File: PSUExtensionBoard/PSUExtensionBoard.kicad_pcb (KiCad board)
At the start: 2 copper layers, 149.9 x 50.8 mm, 14 parts

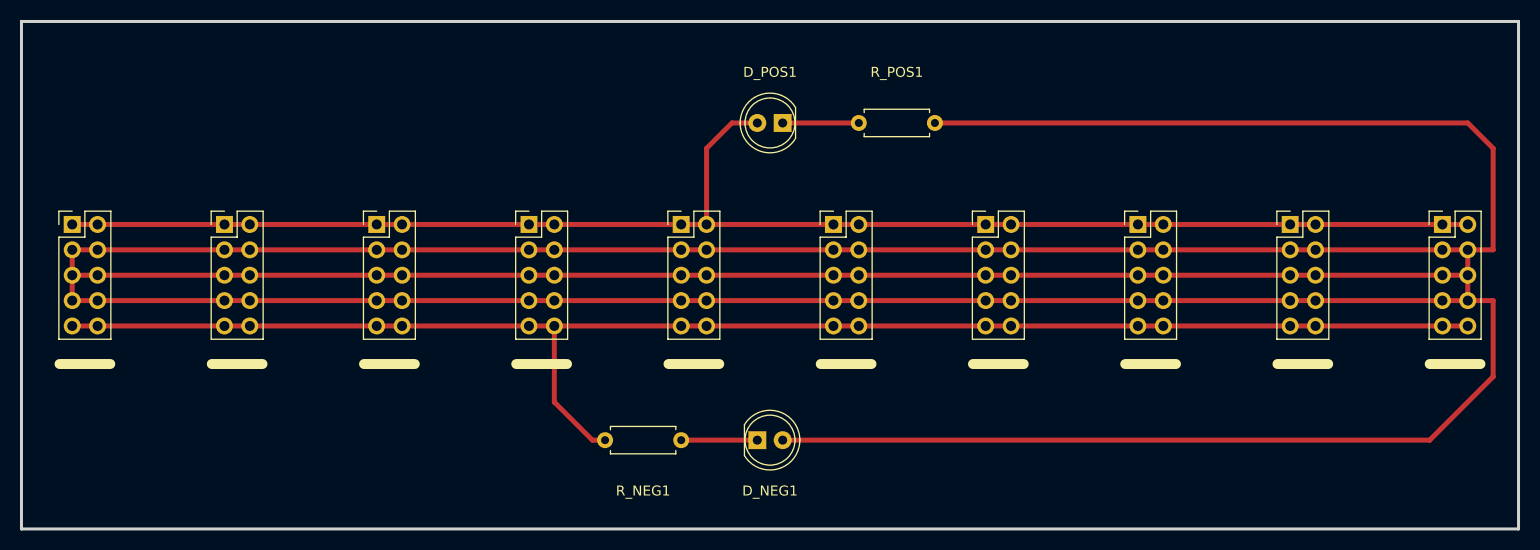
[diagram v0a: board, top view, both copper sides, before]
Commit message: Changed Ext Board to add 5V, CV, Gate
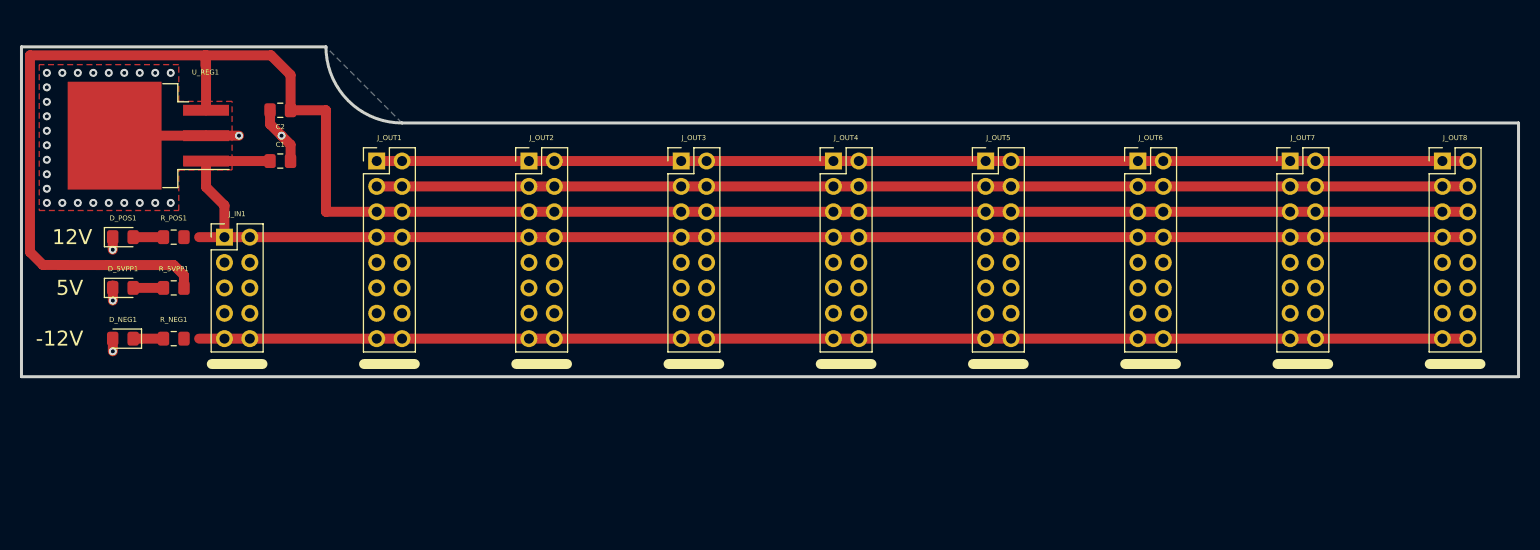
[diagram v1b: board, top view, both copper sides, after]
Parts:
- removed J_OUT10, J_OUT9: Conn_02x05_Odd_Even, Connector_PinHeader_2.54mm:PinHeader_2x05_P2.54mm_Vertical
- added C1: 220nF, Capacitor_SMD:C_0805_2012Metric_Pad1.15x1.40mm_HandSolder, F.Cu at (74.2, 92.7)
- added C2: 100nF, Capacitor_SMD:C_0805_2012Metric_Pad1.15x1.40mm_HandSolder, F.Cu at (74.2, 87.6)
- added D_5VPP1: LED, LED_SMD:LED_0805_2012Metric_Pad1.15x1.40mm_HandSolder, F.Cu at (58.4, 105.4)
- added J_IN1: Conn_02x05_Odd_Even, Connector_PinHeader_2.54mm:PinHeader_2x05_P2.54mm_Vertical, F.Cu at (68.6, 100.3)
- added R_5VPP1: 2K7, Resistor_SMD:R_0805_2012Metric_Pad1.15x1.40mm_HandSolder, F.Cu at (63.5, 105.4)
- added U_REG1: L7805, Package_TO_SOT_SMD:TO-263-3_TabPin2, F.Cu at (61.0, 90.2)
- D_NEG1, D_POS1: footprint LED_THT:LED_D5.0mm -> LED_SMD:LED_0805_2012Metric_Pad1.15x1.40mm_HandSolder
- J_OUT1, J_OUT2, J_OUT3, J_OUT4, J_OUT5, J_OUT6, J_OUT7, J_OUT8: value Conn_02x05_Odd_Even -> Conn_02x08_Odd_Even; footprint Connector_PinHeader_2.54mm:PinHeader_2x05_P2.54mm_Vertical -> Connector_PinHeader_2.54mm:PinHeader_2x08_P2.54mm_Vertical
- R_NEG1, R_POS1: value 1K -> 2K7; footprint Resistor_THT:R_Axial_DIN0207_L6.3mm_D2.5mm_P7.62mm_Horizontal -> Resistor_SMD:R_0805_2012Metric_Pad1.15x1.40mm_HandSolder
- moved R_POS1 69.5 mm to (63.5, 100.3), turned to 180 degrees
- moved D_POS1 67.0 mm to (58.4, 100.3), turned to 0 degrees
- moved D_NEG1 64.3 mm to (58.4, 110.5), turned to 180 degrees
- moved R_NEG1 51.8 mm to (63.5, 110.5), turned to 0 degrees
- moved J_OUT6 31.1 mm to (160.0, 92.7)
- moved J_OUT2 31.1 mm to (99.1, 92.7)
- moved J_OUT3 31.1 mm to (114.3, 92.7)
- moved J_OUT5 31.1 mm to (144.8, 92.7)
- moved J_OUT1 31.1 mm to (83.8, 92.7)
- moved J_OUT4 31.1 mm to (129.5, 92.7)
- moved J_OUT7 31.1 mm to (175.3, 92.7)
- moved J_OUT8 31.1 mm to (190.5, 92.7)
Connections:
- D_POS1 pad 1: Net-(D_POS1-Pad1) -> GND
- J_OUT1 pad 1: Net-(D_POS1-Pad2) -> /GATE
- J_OUT1 pad 10: Net-(J_OUT1-Pad10) -> GND
- J_OUT1 pad 2: Net-(D_POS1-Pad2) -> /GATE
- J_OUT1 pad 3: GND -> /CV
- J_OUT1 pad 4: GND -> /CV
- J_OUT1 pad 5: GND -> /5V
- J_OUT1 pad 6: GND -> /5V
- J_OUT1 pad 7: GND -> /12V
- J_OUT1 pad 8: GND -> /12V
- J_OUT1 pad 9: Net-(J_OUT1-Pad10) -> GND
- J_OUT2 pad 1: Net-(D_POS1-Pad2) -> /GATE
- J_OUT2 pad 10: Net-(J_OUT1-Pad10) -> GND
- J_OUT2 pad 2: Net-(D_POS1-Pad2) -> /GATE
- J_OUT2 pad 3: GND -> /CV
- J_OUT2 pad 4: GND -> /CV
- J_OUT2 pad 5: GND -> /5V
- J_OUT2 pad 6: GND -> /5V
- J_OUT2 pad 7: GND -> /12V
- J_OUT2 pad 8: GND -> /12V
- J_OUT2 pad 9: Net-(J_OUT1-Pad10) -> GND
- J_OUT3 pad 1: Net-(D_POS1-Pad2) -> /GATE
- J_OUT3 pad 10: Net-(J_OUT1-Pad10) -> GND
- J_OUT3 pad 2: Net-(D_POS1-Pad2) -> /GATE
- J_OUT3 pad 3: GND -> /CV
- J_OUT3 pad 4: GND -> /CV
- J_OUT3 pad 5: GND -> /5V
- J_OUT3 pad 6: GND -> /5V
- J_OUT3 pad 7: GND -> /12V
- J_OUT3 pad 8: GND -> /12V
- J_OUT3 pad 9: Net-(J_OUT1-Pad10) -> GND
- J_OUT4 pad 1: Net-(D_POS1-Pad2) -> /GATE
- J_OUT4 pad 10: Net-(J_OUT1-Pad10) -> GND
- J_OUT4 pad 2: Net-(D_POS1-Pad2) -> /GATE
- J_OUT4 pad 3: GND -> /CV
- J_OUT4 pad 4: GND -> /CV
- J_OUT4 pad 5: GND -> /5V
- J_OUT4 pad 6: GND -> /5V
- J_OUT4 pad 7: GND -> /12V
- J_OUT4 pad 8: GND -> /12V
- J_OUT4 pad 9: Net-(J_OUT1-Pad10) -> GND
- J_OUT5 pad 1: Net-(D_POS1-Pad2) -> /GATE
- J_OUT5 pad 10: Net-(J_OUT1-Pad10) -> GND
- J_OUT5 pad 2: Net-(D_POS1-Pad2) -> /GATE
- J_OUT5 pad 3: GND -> /CV
- J_OUT5 pad 4: GND -> /CV
- J_OUT5 pad 5: GND -> /5V
- J_OUT5 pad 6: GND -> /5V
- J_OUT5 pad 7: GND -> /12V
- J_OUT5 pad 8: GND -> /12V
- J_OUT5 pad 9: Net-(J_OUT1-Pad10) -> GND
- J_OUT6 pad 1: Net-(D_POS1-Pad2) -> /GATE
- J_OUT6 pad 10: Net-(J_OUT1-Pad10) -> GND
- J_OUT6 pad 2: Net-(D_POS1-Pad2) -> /GATE
- J_OUT6 pad 3: GND -> /CV
- J_OUT6 pad 4: GND -> /CV
- J_OUT6 pad 5: GND -> /5V
- J_OUT6 pad 6: GND -> /5V
- J_OUT6 pad 7: GND -> /12V
- J_OUT6 pad 8: GND -> /12V
- J_OUT6 pad 9: Net-(J_OUT1-Pad10) -> GND
- J_OUT7 pad 1: Net-(D_POS1-Pad2) -> /GATE
- J_OUT7 pad 10: Net-(J_OUT1-Pad10) -> GND
- J_OUT7 pad 2: Net-(D_POS1-Pad2) -> /GATE
- J_OUT7 pad 3: GND -> /CV
- J_OUT7 pad 4: GND -> /CV
- J_OUT7 pad 5: GND -> /5V
- J_OUT7 pad 6: GND -> /5V
- J_OUT7 pad 7: GND -> /12V
- J_OUT7 pad 8: GND -> /12V
- J_OUT7 pad 9: Net-(J_OUT1-Pad10) -> GND
- J_OUT8 pad 1: Net-(D_POS1-Pad2) -> /GATE
- J_OUT8 pad 10: Net-(J_OUT1-Pad10) -> GND
- J_OUT8 pad 2: Net-(D_POS1-Pad2) -> /GATE
- J_OUT8 pad 3: GND -> /CV
- J_OUT8 pad 4: GND -> /CV
- J_OUT8 pad 5: GND -> /5V
- J_OUT8 pad 6: GND -> /5V
- J_OUT8 pad 7: GND -> /12V
- J_OUT8 pad 8: GND -> /12V
- J_OUT8 pad 9: Net-(J_OUT1-Pad10) -> GND
- R_NEG1 pad 2: Net-(J_OUT1-Pad10) -> /-12V
- R_POS1 pad 1: Net-(D_POS1-Pad1) -> /12V
- R_POS1 pad 2: GND -> Net-(D_POS1-Pad2)
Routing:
- net GND: track 582.8 -> 22.4 mm, vias 0 -> 31
- net /5V: track 0.00 -> 202.4 mm
- net Net-(J_OUT1-Pad10): track 154.0 -> 0.00 mm
- net Net-(D_POS1-Pad2): track 153.5 -> 2.54 mm
- net /12V: track 0.00 -> 141.8 mm
- net /-12V: track 0.00 -> 127.0 mm
- net /GATE: track 0.00 -> 109.2 mm
- net /CV: track 0.00 -> 109.2 mm
- net Net-(D_POS1-Pad1): track 7.62 -> 0.00 mm
- net Net-(D_NEG1-Pad1): track 7.62 -> 2.78 mm
- net Net-(D_5VPP1-Pad2): track 0.00 -> 3.03 mm
- added copper zone on B.Cu, net GND
- added copper zone on F.Cu, net GND
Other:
- board size 149.9 x 50.8 mm -> 149.9 x 33 mm
- board text added: "-12V"
- board text added: "12V"
- board text added: "5V"

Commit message: Created SMT version of AdjustablePSU, RevB
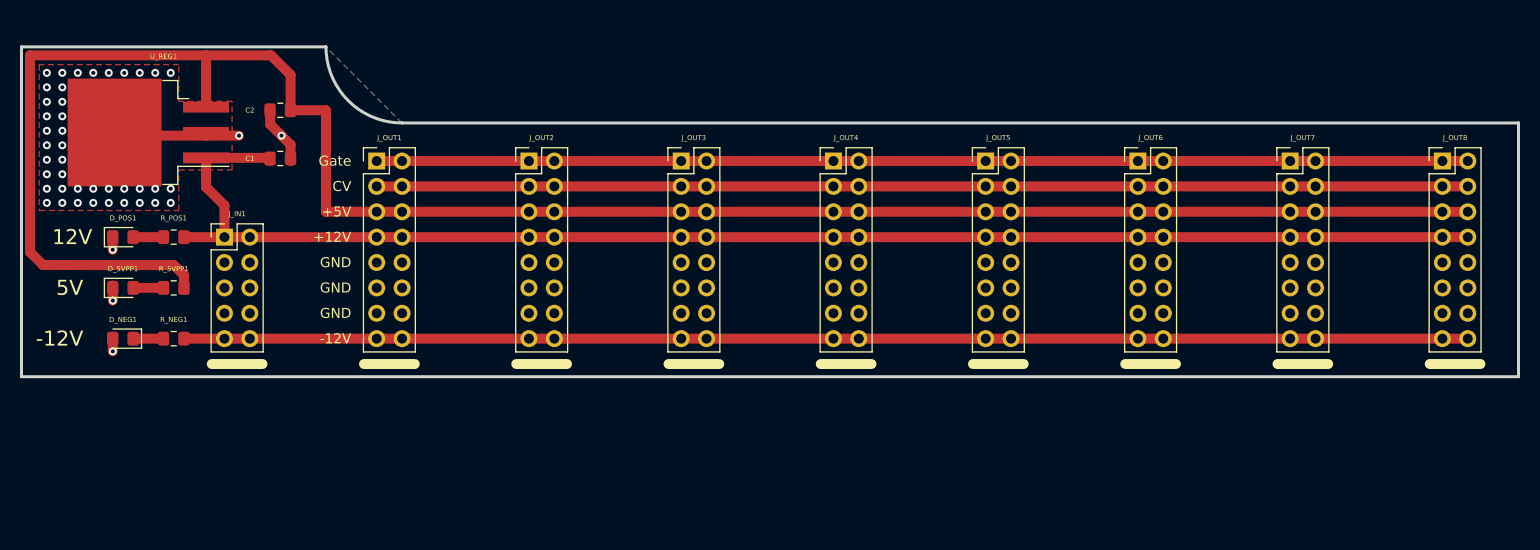
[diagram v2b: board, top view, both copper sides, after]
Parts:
- moved U_REG1 0.32 mm to (61.0, 89.9)
- moved C1 0.25 mm to (74.2, 92.5)
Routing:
- net /12V: track 141.8 -> 143.6 mm
- net /-12V: track 127.0 -> 128.5 mm
- net /5V: track 202.4 -> 201.0 mm
- net GND: vias 31 -> 46
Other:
- board text added: "+/-12V, +5V, CV and Gate"
- board text added: "+12V"
- board text added: "+5V"
- board text added: "CV"
- board text added: "Eurorack PSU Ext. board"
- board text added: "GND"
- board text added: "Gate"
- board text added: "RevA Chris Sutton 2018"
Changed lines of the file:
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@@
   (general
     (thickness 1.6)
-    (drawings 18)
-    (tracks 67)
+    (drawings 29)
+    (tracks 82)
     (zones 0)
     (modules 18)
@@
   )
   (setup
-    (last_trace_width 1)
+    (last_trace_width 0.25)
     (user_trace_width 0.5)
     (user_trace_width 1)
@@
       (outputformat 1)
       (mirror false)
-      (drillshape 1)
+      (drillshape 0)
       (scaleselection 1)
-      (outputdirectory ""))
+      (outputdirectory "PSUEXT_GERBER/"))
   )
   (net 0 "")
@@
   )
   (module Package_TO_SOT_SMD:TO-263-3_TabPin2 (layer F.Cu)
-    (at 60.96 90.17 180)
+    (at 60.96 89.8525 180)
     (descr "TO-263 / D2PAK / DDPAK SMD package, http://www.infineon.com/cms/en/product/packages/PG-TO263/PG-TO263-3-1/")
     (tags "D2PAK DDPAK TO-263 D2PAK-3 TO-263-3 SOT-404")
     (attr smd)
-    (fp_text reference U_REG1 (at -5.715 6.35 180) (layer F.SilkS)
+    (fp_text reference U_REG1 (at -1.524 7.62 180) (layer F.SilkS)
       (effects (font (size 0.5 0.5) (thickness 0.1)))
     )
@@
   )
   (module Capacitor_SMD:C_0805_2012Metric_Pad1.15x1.40mm_HandSolder (layer F.Cu)
-    (at 74.168 92.71)
+    (at 74.168 92.456)
     (descr "Capacitor SMD 0805 (2012 Metric), square (rectangular) end terminal, IPC_7351 nominal with elongated pad for handsoldering. (Body size source: https://docs.google.com/spreadsheets/d/1BsfQQcO9C6DZCsRaXUlFlo91Tg2WpOkGARC1WS5S8t0/edit?usp=sharing), generated with kicad-footprint-generator")
     (tags "capacitor handsolder")
     (attr smd)
-    (fp_text reference C1 (at 0 -1.65) (layer F.SilkS)
+    (fp_text reference C1 (at -3.048 0) (layer F.SilkS)
       (effects (font (size 0.5 0.5) (thickness 0.1)))
     )
@@
     (tags "capacitor handsolder")
     (attr smd)
-    (fp_text reference C2 (at 0 -1.65 180) (layer F.SilkS)
+    (fp_text reference C2 (at 3.048 0 180) (layer F.SilkS)
       (effects (font (size 0.5 0.5) (thickness 0.1)))
     )
@@
     )
   )
+  (gr_text -12V (at 81.28 110.49) (layer F.SilkS)
+    (effects (font (size 1 1) (thickness 0.2)) (justify right))
+  )
+  (gr_text GND (at 81.28 107.95) (layer F.SilkS)
+    (effects (font (size 1 1) (thickness 0.2)) (justify right))
+  )
+  (gr_text GND (at 81.28 105.41) (layer F.SilkS)
+    (effects (font (size 1 1) (thickness 0.2)) (justify right))
+  )
+  (gr_text GND (at 81.28 102.87) (layer F.SilkS)
+    (effects (font (size 1 1) (thickness 0.2)) (justify right))
+  )
+  (gr_text +12V (at 81.28 100.33) (layer F.SilkS)
+    (effects (font (size 1 1) (thickness 0.2)) (justify right))
+  )
+  (gr_text +5V (at 81.28 97.79) (layer F.SilkS)
+    (effects (font (size 1 1) (thickness 0.2)) (justify right))
+  )
+  (gr_text CV (at 81.28 95.25) (layer F.SilkS)
+    (effects (font (size 1 1) (thickness 0.2)) (justify right))
+  )
+  (gr_text Gate (at 81.28 92.71) (layer F.SilkS)
+    (effects (font (size 1 1) (thickness 0.2)) (justify right))
+  )
+  (gr_text "RevA Chris Sutton 2018" (at 80.2005 101.6 90) (layer B.SilkS)
+    (effects (font (size 1 1) (thickness 0.2)) (justify mirror))
+  )
+  (gr_text "+/-12V, +5V, CV and Gate" (at 77.47 101.6 90) (layer B.SilkS)
+    (effects (font (size 1 1) (thickness 0.2)) (justify mirror))
+  )
+  (gr_text "Eurorack PSU Ext. board" (at 74.93 101.6 90) (layer B.SilkS)
+    (effects (font (size 1 1) (thickness 0.2)) (justify mirror))
+  )
   (gr_line (start 48.26 81.28) (end 78.74 81.28) (layer Edge.Cuts) (width 0.3))
   (gr_line (start 86.36 88.9) (end 198.12 88.9) (layer Edge.Cuts) (width 0.3))
   (gr_arc (start 86.36 81.28) (end 78.74 81.28) (angle -90) (layer Edge.Cuts) (width 0.3))
   (gr_text -12V (at 52.07 110.49) (layer F.SilkS)
-    (effects (font (size 1.5 1.5) (thickness 0.3)))
+    (effects (font (size 1.5 1.5) (thickness 0.2)))
   )
   (gr_text 5V (at 53.086 105.41) (layer F.SilkS)
-    (effects (font (size 1.5 1.5) (thickness 0.3)))
+    (effects (font (size 1.5 1.5) (thickness 0.2)))
   )
   (gr_text 12V (at 53.34 100.33) (layer F.SilkS)
-    (effects (font (size 1.5 1.5) (thickness 0.3)))
+    (effects (font (size 1.5 1.5) (thickness 0.2)))
   )
   (gr_line (start 189.23 113.03) (end 194.31 113.03) (layer F.SilkS) (width 1))
@@
   (segment (start 57.404 105.165) (end 57.404 106.68) (width 1) (layer F.Cu) (net 1))
   (via (at 57.404 106.68) (size 0.8) (drill 0.4) (layers F.Cu B.Cu) (net 1))
+  (via (at 52.35 85.3335) (size 0.8) (drill 0.4) (layers F.Cu B.Cu) (net 1))
+  (via (at 52.35 86.7835) (size 0.8) (drill 0.4) (layers F.Cu B.Cu) (net 1))
+  (via (at 52.35 88.2335) (size 0.8) (drill 0.4) (layers F.Cu B.Cu) (net 1))
+  (via (at 52.35 89.6835) (size 0.8) (drill 0.4) (layers F.Cu B.Cu) (net 1))
+  (via (at 52.35 91.1335) (size 0.8) (drill 0.4) (layers F.Cu B.Cu) (net 1))
+  (via (at 52.35 92.5835) (size 0.8) (drill 0.4) (layers F.Cu B.Cu) (net 1))
+  (via (at 52.35 94.0335) (size 0.8) (drill 0.4) (layers F.Cu B.Cu) (net 1))
+  (via (at 52.35 95.4835) (size 0.8) (drill 0.4) (layers F.Cu B.Cu) (net 1))
+  (via (at 53.9 95.4835) (size 0.8) (drill 0.4) (layers F.Cu B.Cu) (net 1))
+  (via (at 55.45 95.4835) (size 0.8) (drill 0.4) (layers F.Cu B.Cu) (net 1))
+  (via (at 57 95.4835) (size 0.8) (drill 0.4) (layers F.Cu B.Cu) (net 1))
+  (via (at 58.55 95.4835) (size 0.8) (drill 0.4) (layers F.Cu B.Cu) (net 1))
+  (via (at 60.1 95.4835) (size 0.8) (drill 0.4) (layers F.Cu B.Cu) (net 1))
+  (via (at 61.65 95.4835) (size 0.8) (drill 0.4) (layers F.Cu B.Cu) (net 1))
+  (via (at 63.2 95.4835) (size 0.8) (drill 0.4) (layers F.Cu B.Cu) (net 1))
   (segment (start 59.445 110.49) (end 62.23 110.49) (width 1) (layer F.Cu) (net 2))
   (segment (start 59.69 100.33) (end 62.23 100.33) (width 1) (layer F.Cu) (net 3))
-  (segment (start 66.735 92.71) (end 73.143 92.71) (width 1) (layer F.Cu) (net 4))
-  (segment (start 66.735 92.71) (end 66.735 95.31) (width 1) (layer F.Cu) (net 4))
-  (segment (start 68.58 97.155) (end 68.58 100.33) (width 1) (layer F.Cu) (net 4))
-  (segment (start 66.735 95.31) (end 68.58 97.155) (width 1) (layer F.Cu) (net 4))
-  (segment (start 66.04 100.33) (end 193.04 100.33) (width 1) (layer F.Cu) (net 4))
+  (segment (start 66.735 95.31) (end 66.7385 92.3925) (width 1) (layer F.Cu) (net 4))
+  (segment (start 68.58 97.155) (end 66.735 95.31) (width 1) (layer F.Cu) (net 4))
+  (segment (start 68.58 100.33) (end 68.58 97.155) (width 1) (layer F.Cu) (net 4))
+  (segment (start 72.8255 92.3925) (end 73.143 92.71) (width 1) (layer F.Cu) (net 4))
+  (segment (start 66.735 92.3925) (end 72.8255 92.3925) (width 1) (layer F.Cu) (net 4))
+  (segment (start 64.643 100.33) (end 193.04 100.33) (width 1) (layer F.Cu) (net 4))
   (segment (start 83.82 97.79) (end 193.04 97.79) (width 1) (layer F.Cu) (net 5))
   (segment (start 75.193 87.63) (end 78.74 87.63) (width 1) (layer F.Cu) (net 5))
@@
   (segment (start 73.24001 82.13001) (end 75.193 84.083) (width 1) (layer F.Cu) (net 5))
   (segment (start 66.675 82.13001) (end 73.24001 82.13001) (width 1) (layer F.Cu) (net 5))
-  (segment (start 66.675 83.185) (end 66.675 82.13001) (width 1) (layer F.Cu) (net 5))
-  (segment (start 66.735 82.13001) (end 66.735 87.63) (width 1) (layer F.Cu) (net 5))
+  (segment (start 66.735 82.13001) (end 66.7385 87.3125) (width 1) (layer F.Cu) (net 5))
   (segment (start 49.11001 82.13001) (end 66.735 82.13001) (width 1) (layer F.Cu) (net 5))
   (segment (start 49.11001 101.81501) (end 49.11001 82.13001) (width 1) (layer F.Cu) (net 5))
   (segment (start 50.41 103.115) (end 49.11001 101.81501) (width 1) (layer F.Cu) (net 5))
   (segment (start 56.896 103.124) (end 50.41 103.115) (width 1) (layer F.Cu) (net 5))
-  (segment (start 56.896 103.124) (end 63.5 103.124) (width 1) (layer F.Cu) (net 5))
-  (segment (start 64.525 104.149) (end 64.525 105.41) (width 1) (layer F.Cu) (net 5))
-  (segment (start 63.5 103.124) (end 64.525 104.149) (width 1) (layer F.Cu) (net 5))
+  (segment (start 63.5 103.124) (end 56.896 103.124) (width 1) (layer F.Cu) (net 5))
+  (segment (start 64.525 104.149) (end 63.5 103.124) (width 1) (layer F.Cu) (net 5))
+  (segment (start 64.525 105.41) (end 64.525 104.149) (width 1) (layer F.Cu) (net 5))
   (segment (start 59.445 105.41) (end 62.475 105.41) (width 1) (layer F.Cu) (net 6))
-  (segment (start 66.04 110.49) (end 193.04 110.49) (width 1) (layer F.Cu) (net 7))
+  (segment (start 64.5795 110.49) (end 193.04 110.49) (width 1) (layer F.Cu) (net 7))
   (segment (start 83.82 92.71) (end 193.04 92.71) (width 1) (layer F.Cu) (net 8))
   (segment (start 193.04 95.25) (end 83.82 95.25) (width 1) (layer F.Cu) (net 9))
